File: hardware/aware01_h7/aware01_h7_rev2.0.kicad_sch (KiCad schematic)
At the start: 60 parts, among them J1 Conn_01x06_Pin, J2 Conn_01x03_Pin, SW1 SW_Push, U1 STM32H7B0ZBTx, U2 IS45S16800F-7TLA2, Y1 WE-XTAL 24.0MHz 50ppm

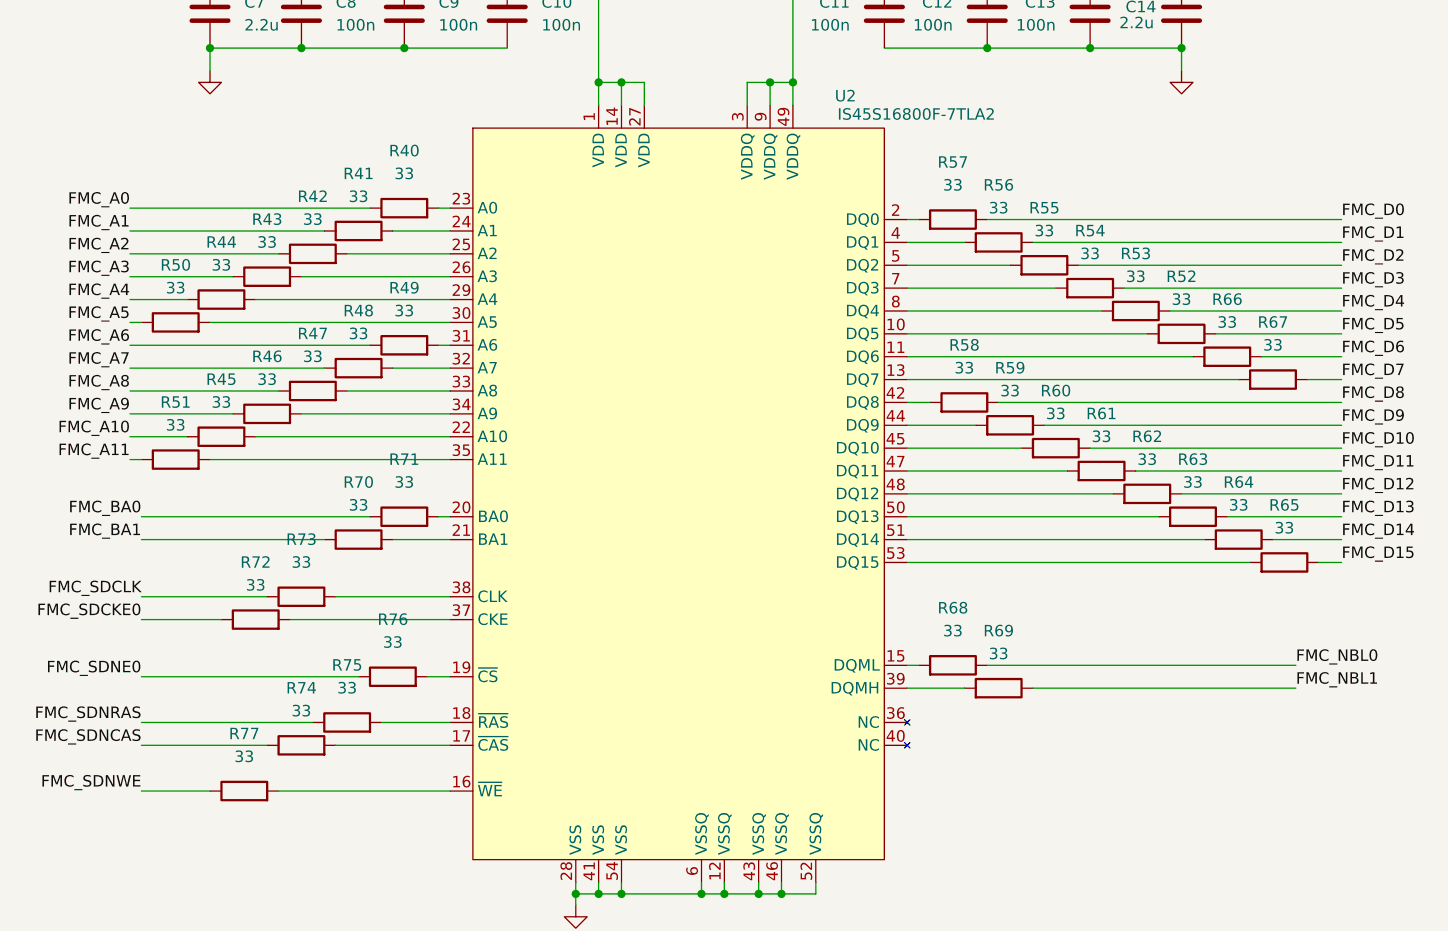
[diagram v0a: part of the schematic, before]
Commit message: add series termination resistors
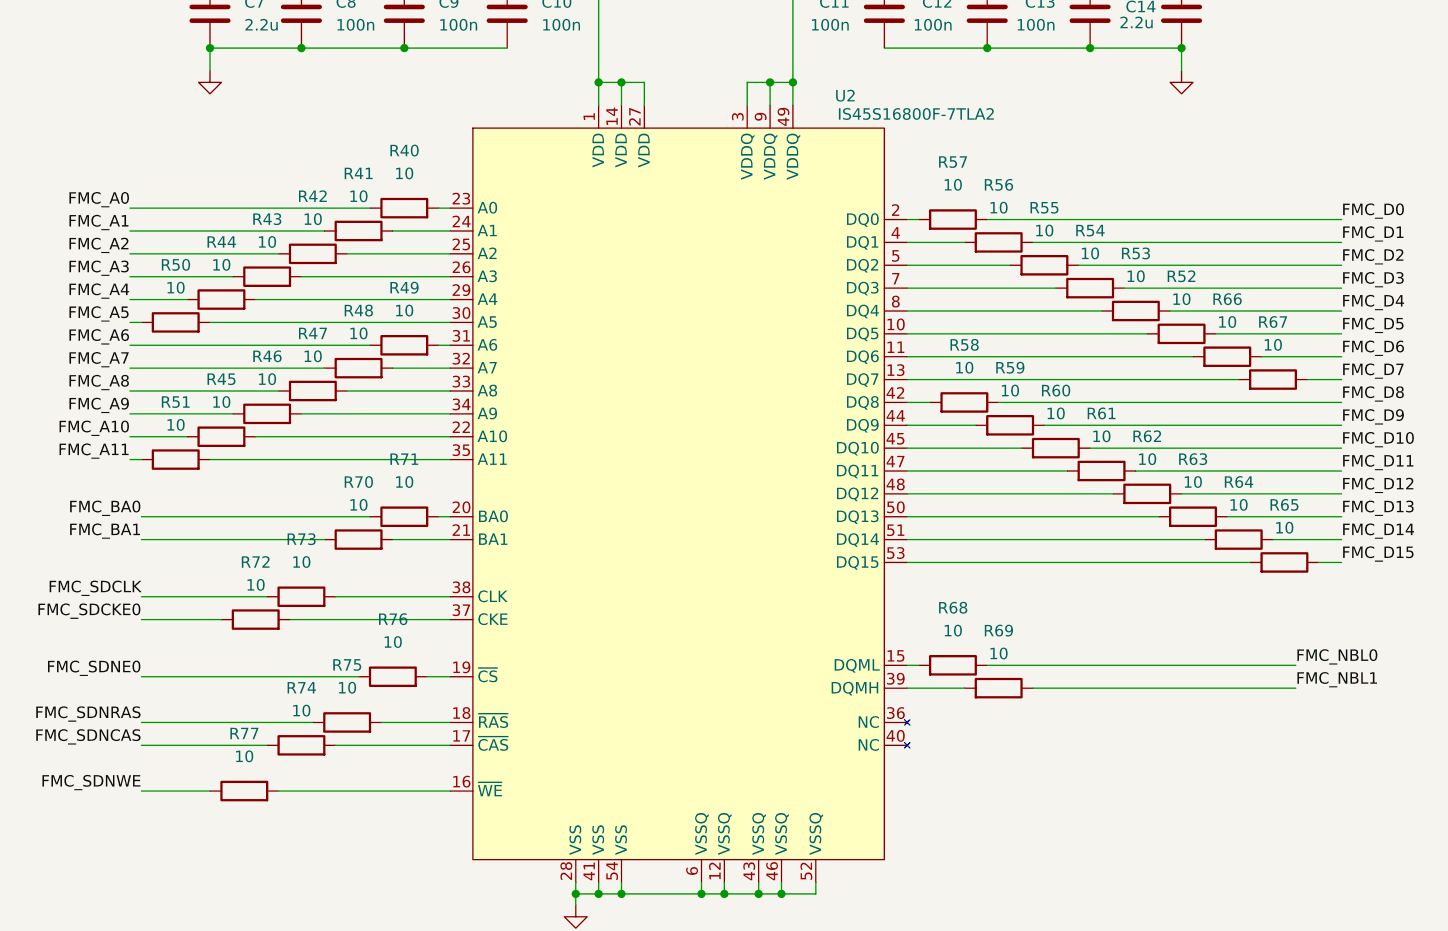
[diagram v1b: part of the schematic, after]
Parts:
- R40, R41, R42, R43, R44, R45, R46, R47, R48, R49, R50, R51, R52, R53, R54, R55, R56, R57, R58, R59, R60, R61, R62, R63, R64, R65, R66, R67, R68, R69, R70, R71, R72, R73, R74, R75, R76, R77: value 33 -> 10; footprint Resistor_SMD:R_0402_1005Metric_Pad0.72x0.64mm_HandSolder -> (none); Manufacturer_Name Susumu -> (none); Manufacturer_Part_Number RG1005R-330-D-T10 -> (none); Mouser Part Number 754-RG1005R-330DT10 -> (none)
